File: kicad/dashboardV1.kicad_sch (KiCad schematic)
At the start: 1 part

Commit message: save
save
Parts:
- added J1, J2: Conn_01x01, TerminalBlock_Wuerth:Wuerth_REDCUBE-THR_WP-THRBU_74655095_THR, symbol Connector_Generic:Conn_01x01
- added J3, J5: Conn_01x05_Female, Connector_Molex:Molex_MicroClasp_55932-0530_1x05_P2.00mm_Vertical, symbol Connector:Conn_01x05_Female
- added J4: Conn_01x02_Female, Connector_Molex:Molex_MicroClasp_55932-0230_1x02_P2.00mm_Vertical, symbol Connector:Conn_01x02_Female
- XA1: renamed from XA?; footprint (none) -> Arduino:Arduino_Mega2560_Shield
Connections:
- net On/off RPI: now also XA1.D52
- net sig_left_deploy: now reaches XA1.D10
- net sig_right_deploy: now reaches XA1.D11
- net sig_left_retract: now reaches XA1.D12
- net sig_right_retract: now reaches XA1.D13
- net sig_rear_defrost: now reaches XA1.D2 (D2_INT0)
- net sig_radiator_fan: now reaches XA1.D24
- net sig_efi_relay: now reaches XA1.D25
- net sig_fuel_pump: now reaches XA1.D26
- net sig_gauges: now reaches XA1.D28
- net sig_front_defrost: now reaches XA1.D3 (D3_INT1)
- net sig_starter: now reaches XA1.D31
- net sig_horn: now reaches XA1.D32
- net sig_reverse_light: now reaches XA1.D34
- net sig_rear_fog_light: now reaches XA1.D35
- net sig_exterior_lights: now reaches XA1.D36
- net sig_high_beam: now reaches XA1.D37
- net sig_low_beam: now reaches XA1.D38
- net sig_front_wipers: now reaches XA1.D4
- net sig_left_turn_signal: now reaches XA1.D40
- net sig_right_turn_signal: now reaches XA1.D41
- net sig_speaker: now reaches XA1.D44
- net sig_left_window_up: now reaches XA1.D5
- net sig_left_window_down: now reaches XA1.D6
- net sig_right_window_up: now reaches XA1.D7
- net sig_right_window_down: now reaches XA1.D8
- new net +12V: J1.1 (Pin_1)
- new net GND: J2.1 (Pin_1)
- new net acc_switch: J5.3 (Pin_3)
- new net brake_switch: J5.5 (Pin_5)
- new net egt_sensor: J3.3 (Pin_3)
- new net fuel_level_sensor: J3.2 (Pin_2)
- new net ign_switch: J5.2 (Pin_2)
- new net intake_t_sensor: J3.1 (Pin_1)
- new net oil_p_sensor: J3.4 (Pin_4)
- new net oil_t_sensor: J3.5 (Pin_5)
- new net reverse_switch: J5.4 (Pin_4)
- new net start_switch: J5.1 (Pin_1)
- new net steering_turn_left_sig: J4.2 (Pin_2)
- new net steering_turn_right_sig: J4.1 (Pin_1)
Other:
- added sheet POWER_SWITCH (12V_output.kicad_sch)
- added sheet SPEAKER_DRIVER (speaker-driver.kicad_sch)

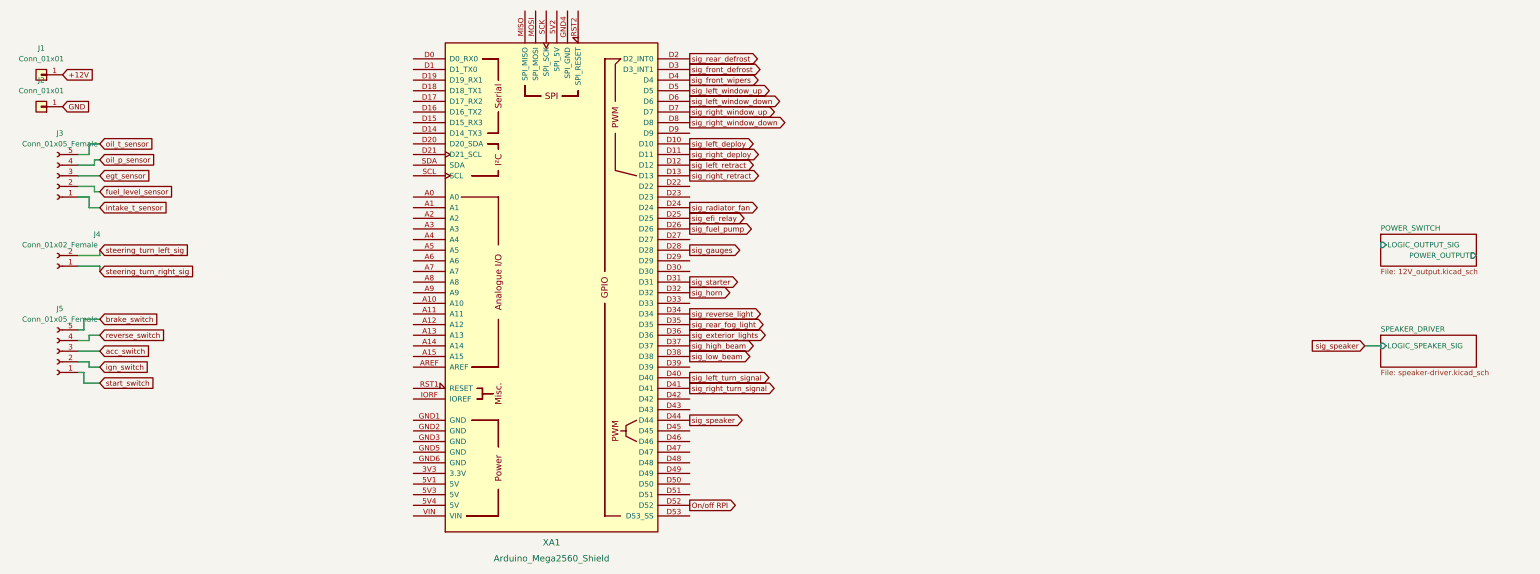
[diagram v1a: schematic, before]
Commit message: front : created base UI
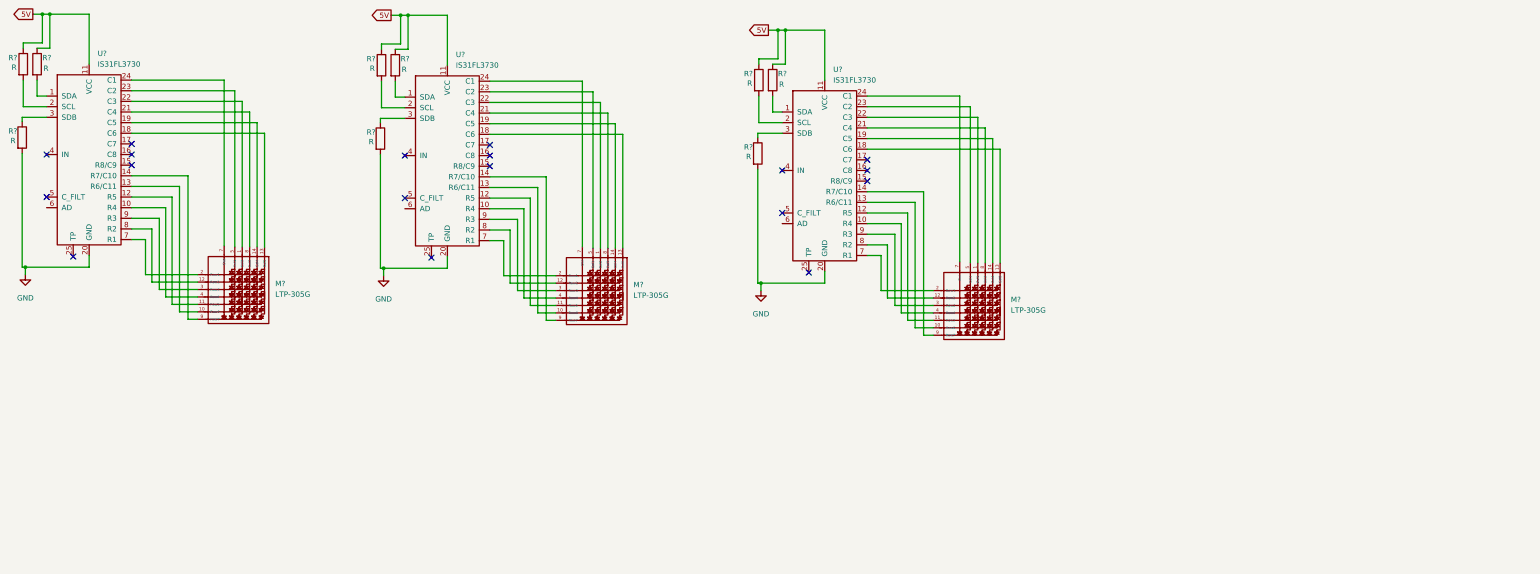
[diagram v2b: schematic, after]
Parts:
- removed J1, J2: Conn_01x01, TerminalBlock_Wuerth:Wuerth_REDCUBE-THR_WP-THRBU_74655095_THR, symbol Connector_Generic:Conn_01x01
- removed J3, J5: Conn_01x05_Female, Connector_Molex:Molex_MicroClasp_55932-0530_1x05_P2.00mm_Vertical, symbol Connector:Conn_01x05_Female
- removed J4: Conn_01x02_Female, Connector_Molex:Molex_MicroClasp_55932-0230_1x02_P2.00mm_Vertical, symbol Connector:Conn_01x02_Female
- removed XA1: Arduino_Mega2560_Shield, Arduino:Arduino_Mega2560_Shield, symbol arduino:Arduino_Mega2560_Shield
- added M? (x3): LTP-305G, symbol ltp-305g:LTP-305G
- added R? (x9): R, symbol Device:R
- added U? (x3): IS31FL3730, Package_DFN_QFN:QFN-24-1EP_4x4mm_P0.5mm_EP2.6x2.6mm, symbol IS31FL3730:IS31FL3730
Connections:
- net GND: now also R?.2, R?.2, R?.2, U?.20 (GND), U?.20 (GND), U?.20 (GND)
- new net: M?.1 (Col2), U?.22 (C3) (x3)
- new net: M?.10 (Row6), U?.13 (R6/C11) (x3)
- new net: M?.11 (Row5), U?.12 (R5) (x3)
- new net: M?.12 (Row2), U?.8 (R2) (x3)
- new net: M?.13 (Col5), U?.18 (C6) (x3)
- new net: M?.14 (Col4), U?.19 (C5) (x3)
- new net: M?.2 (Row1), U?.7 (R1) (x3)
- new net: M?.3 (Row3), U?.9 (R3) (x3)
- new net: M?.4 (Row4), U?.10 (R4) (x3)
- new net: M?.5 (Col1), U?.23 (C2) (x3)
- new net: M?.7 (Dot), U?.24 (C1) (x3)
- new net: M?.8 (Col3), U?.21 (C4) (x3)
- new net: M?.9 (Row7), U?.14 (R7/C10) (x3)
- new net: R?.2, U?.1 (SDA) (x3)
- new net: R?.2, U?.2 (SCL) (x3)
- new net: R?.1, U?.3 (SDB) (x3)
- new net 5V: R?.1, R?.1, R?.1, R?.1, R?.1, R?.1, U?.11 (VCC), U?.11 (VCC), U?.11 (VCC)
- no-connect marks 0 -> 18
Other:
- removed sheet POWER_SWITCH
- removed sheet SPEAKER_DRIVER
